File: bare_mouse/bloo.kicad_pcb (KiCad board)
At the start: 2 copper layers, 100 x 105.9 mm, 99 parts, among them J1 Serial Debug Header, J10 Conn_01x06_Female, J2 SWD Header, J4 Conn_ARM_JTAG_SWD_10, J5 SWD Header, M1 M1_Conn_Alt, M2 M2_Conn_Alt, Q0 TEFT4300, Q1 TEFT4300, Q10 Q_NMOS_GSD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

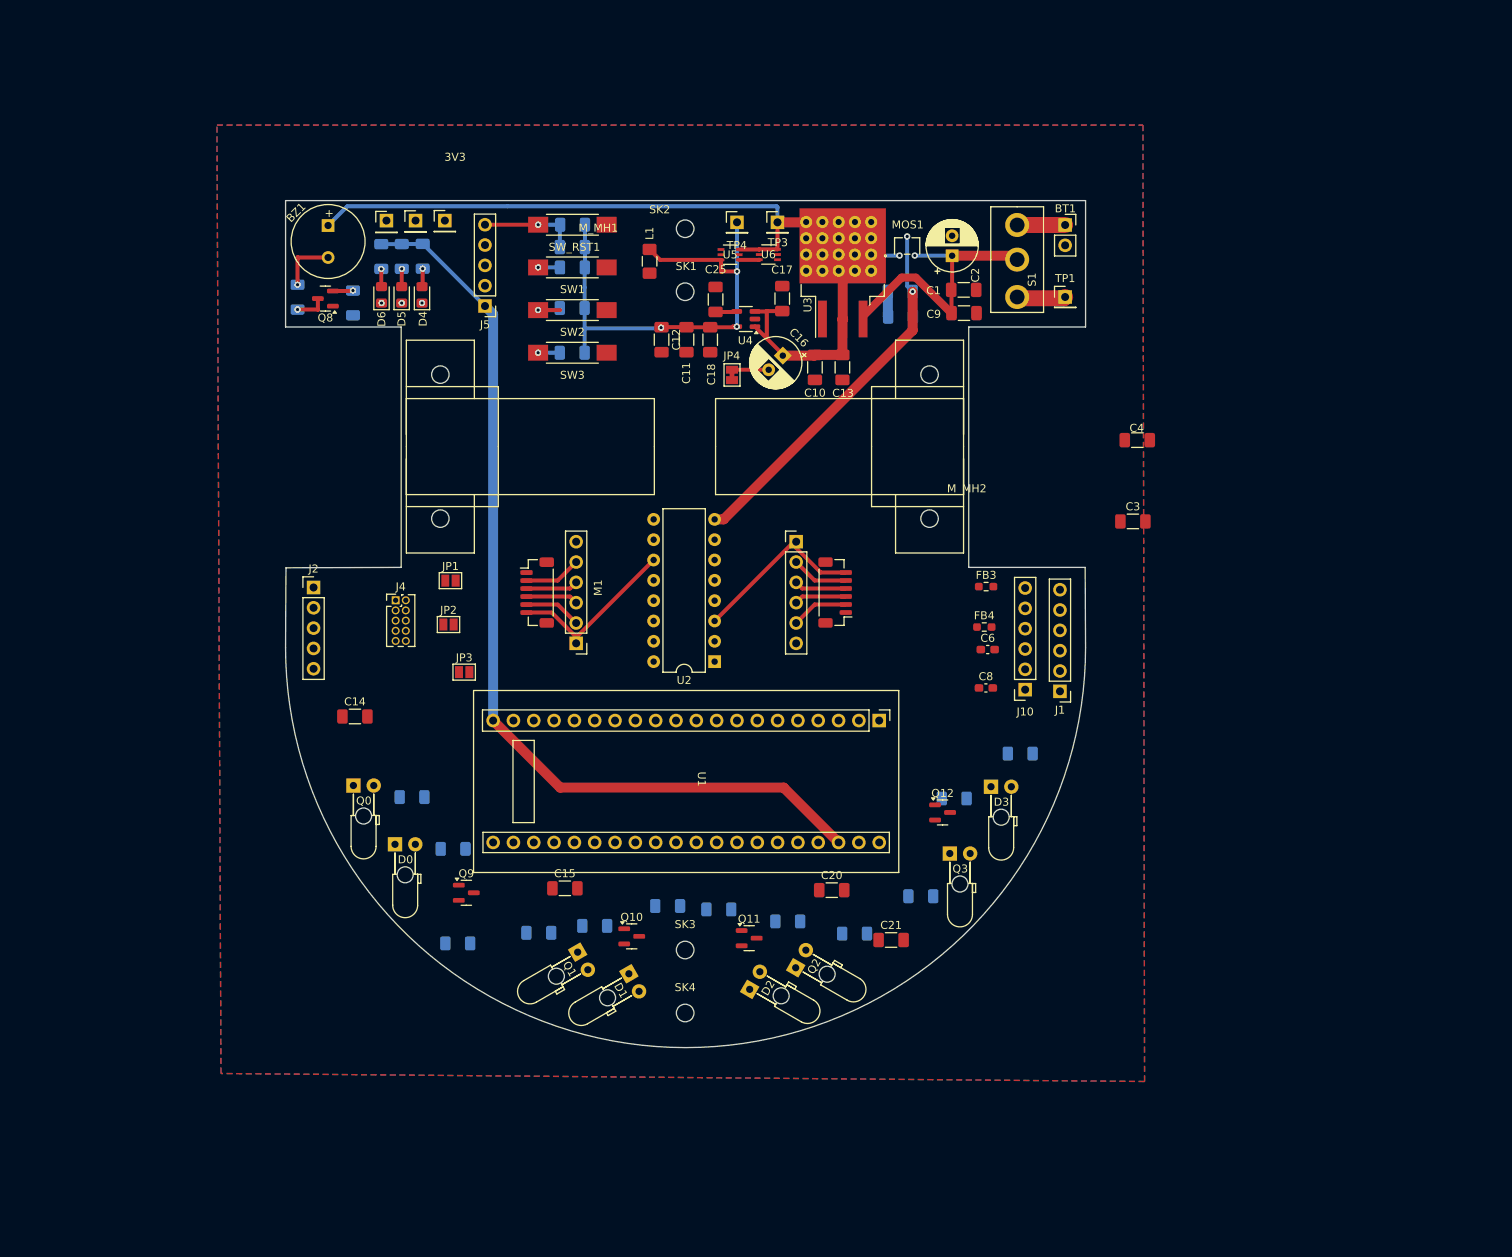
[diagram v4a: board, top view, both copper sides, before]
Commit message: Finished routing, DRC shows 8 errors having to do with SWD header module
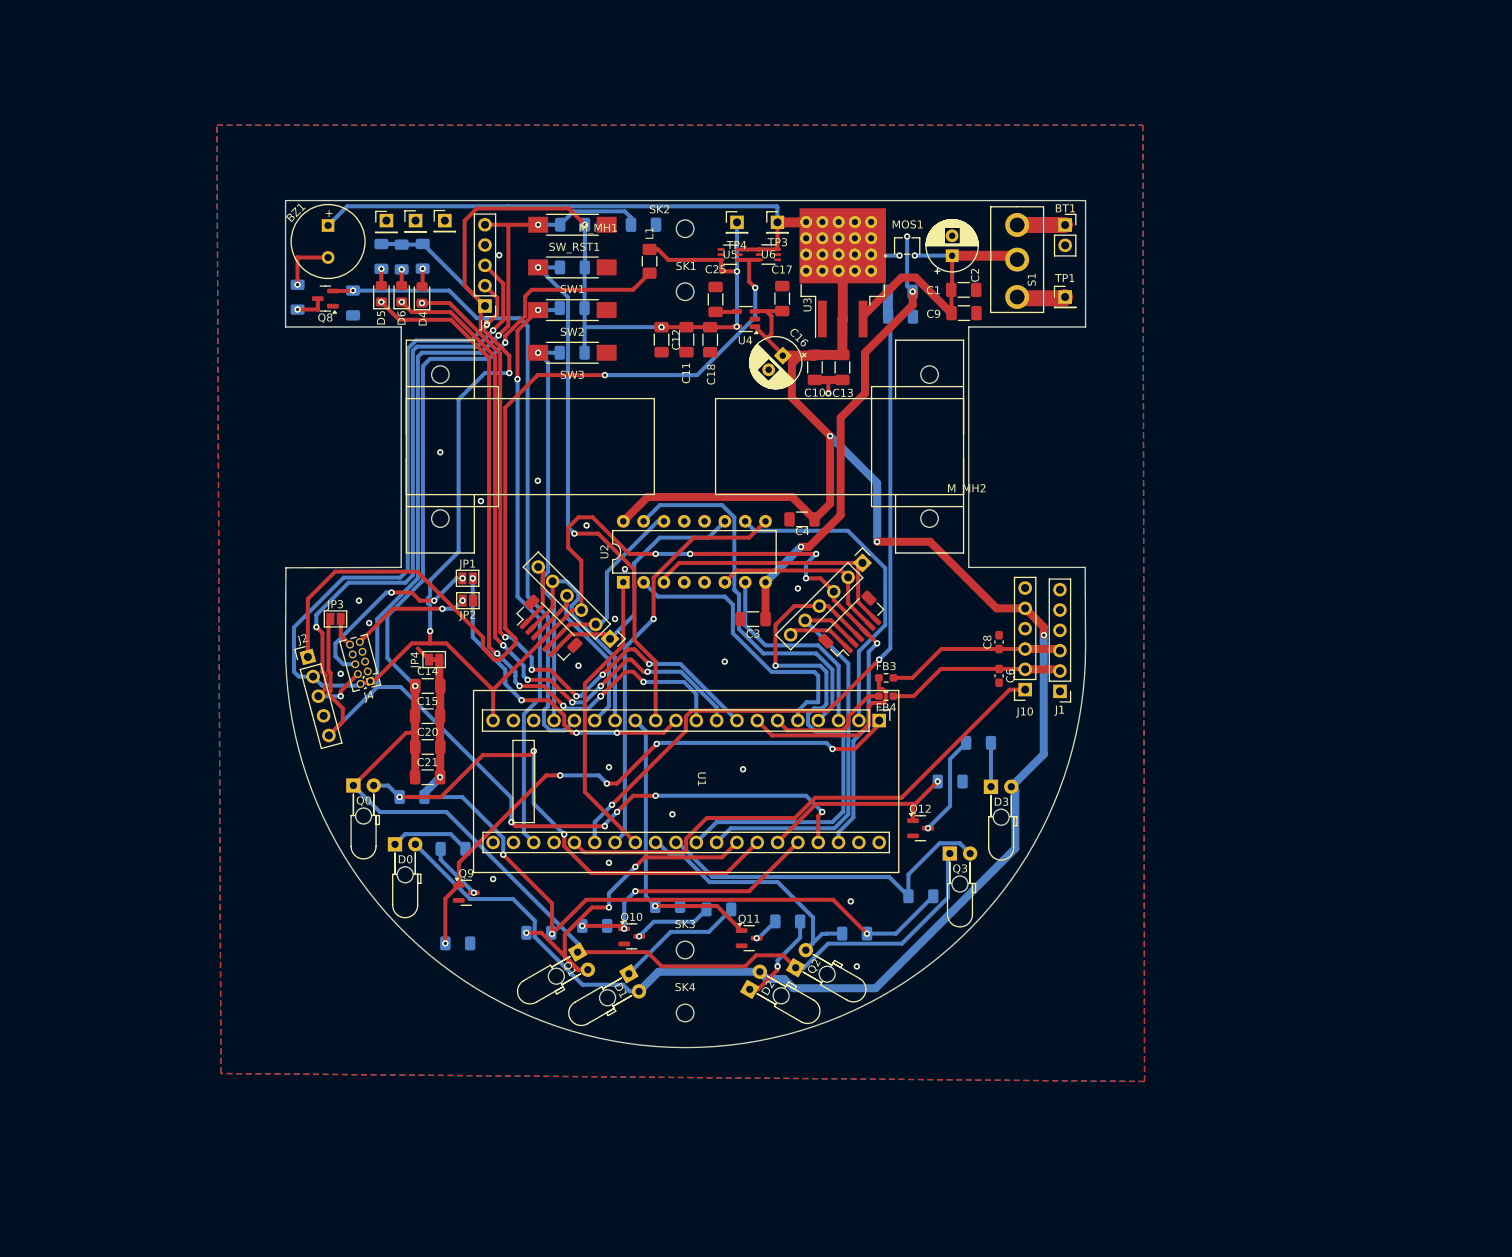
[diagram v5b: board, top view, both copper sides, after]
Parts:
- moved C21 61.4 mm to (178.5, 162.5)
- moved C20 53.6 mm to (178.5, 158.8)
- moved JP4 51.5 mm to (179.3, 147.8), turned to 0 degrees
- moved C3 49.0 mm to (219.2, 142.8), turned to 180 degrees
- moved C4 43.1 mm to (225.3, 130.3), turned to 180 degrees
- moved C15 27.5 mm to (178.5, 154.9)
- moved JP3 17.4 mm to (167.0, 142.7)
- moved FB3 16.9 mm to (235.8, 150.1)
- moved U2 15.1 mm to (203.0, 138.2), turned to 90 degrees
- moved FB4 15.0 mm to (235.8, 152.4), turned to 180 degrees
- moved J4 10.6 mm to (171.3, 150.5), turned to -165 degrees
- moved C14 9.87 mm to (178.5, 151.1)
- moved C19 9.32 mm to (205.5, 93.5)
- moved J2 8.71 mm to (163.5, 147.5), turned to 15 degrees
- moved C8 5.97 mm to (249.9, 145.6), turned to 90 degrees
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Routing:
- net +5V_NET: track 106.1 -> 320.0 mm, vias 1 -> 4
- net +3.3VA: track 0.00 -> 195.0 mm, vias 0 -> 2
- net RST: track 12.2 -> 185.5 mm, vias 1 -> 7
- net +3V3_NET: track 2.52 -> 116.8 mm, vias 0 -> 2
- net AGND: track 0.00 -> 97.7 mm, vias 0 -> 4
- net +3V3: track 192.3 -> 284.2 mm, vias 3 -> 11
- net V_METER: track 3.15 -> 94.5 mm, vias 0 -> 2
- net LED_GREEN: track 0.00 -> 88.7 mm, vias 1 -> 7
- net LED_BLUE: track 0.00 -> 87.7 mm, vias 1 -> 6
- net LED_RED: track 0.00 -> 87.1 mm, vias 1 -> 6
- net SWDCLK: track 0.00 -> 80.3 mm, vias 0 -> 3
- net BUZZER: track 2.53 -> 81.9 mm
- net SWDIO: track 0.00 -> 76.7 mm, vias 0 -> 1
- net EMIT_1: track 0.00 -> 72.6 mm, vias 0 -> 5
- net BUTTON_2: track 5.57 -> 73.5 mm, vias 1 -> 2
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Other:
- board text removed: "3V3"

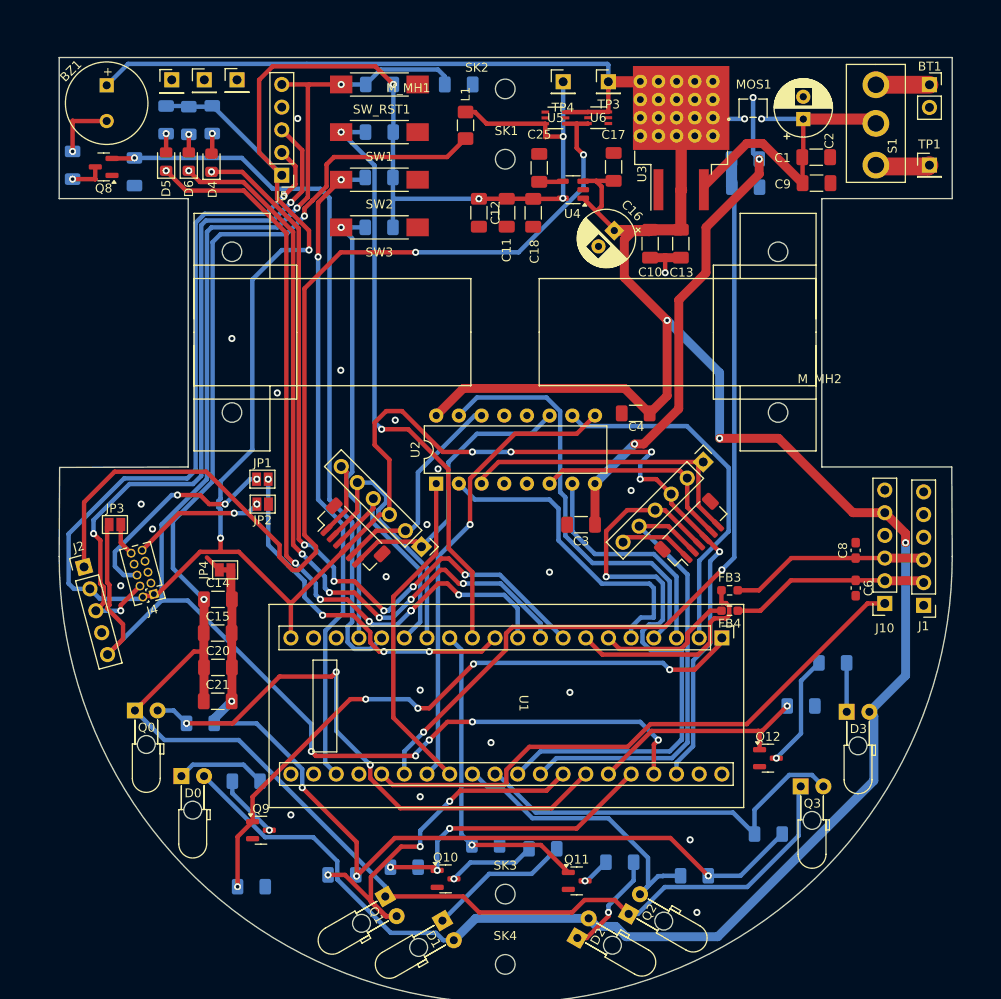
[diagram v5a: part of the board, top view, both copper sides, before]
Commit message: Finished routing the mouse, referenced design notes to finalize silkscreen, rearranged SWD header module to fix previous errors - current final draft of the rat
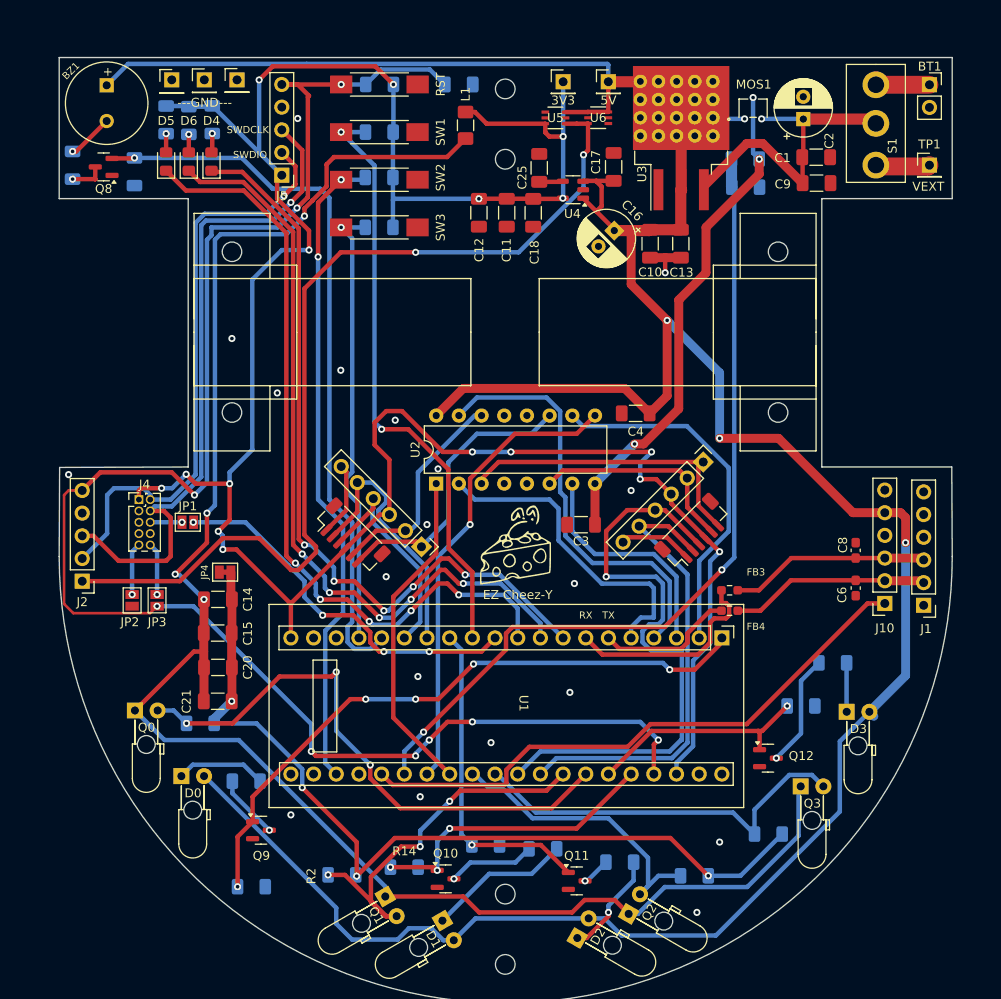
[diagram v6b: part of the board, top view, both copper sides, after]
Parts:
- added G***: LOGO, LOGO, F.Cu at (211.8, 145.7)
- moved JP2 18.2 mm to (168.9, 151.2), turned to 90 degrees
- moved J4 10.7 mm to (169.7, 140.0), turned to 0 degrees
- moved JP3 9.71 mm to (171.7, 151.2), turned to 90 degrees
- moved JP1 9.65 mm to (175.1, 142.5)
- moved J2 1.61 mm to (163.3, 149.1), turned to 180 degrees
- moved JP4 0.25 mm to (179.3, 148.1)
- moved D4 0.13 mm to (177.8, 102.1)
- renumbered SW_RST1 to RST
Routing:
- net Net-(J4-SWO/TDO): track 24.6 -> 3.56 mm, vias 3 -> 1
- net SWDIO: track 76.7 -> 65.8 mm
- net +3V3_NET: track 116.8 -> 106.4 mm
- net Net-(J4-GNDDetect): track 15.0 -> 5.87 mm, vias 2 -> 1
- net SWDCLK: track 80.3 -> 74.4 mm, vias 3 -> 1
- net RST: track 185.5 -> 189.4 mm, vias 7 -> 9
- net +3V3: track 284.2 -> 281.8 mm, vias 11 -> 16
- net Net-(J4-~{RESET}): track 3.69 -> 5.87 mm, vias 0 -> 1
- net SWO: track 40.1 -> 42.2 mm
- net Net-(BZ1-+): track 7.27 -> 5.23 mm
- net GND: track 23.6 -> 21.6 mm, vias 18 -> 19
- net +5V_NET: track 320.0 -> 321.4 mm
- net EMIT_1: track 72.6 -> 71.8 mm
- net LED_RED: track 87.1 -> 87.2 mm, vias 6 -> 5
- net +3.3VA: track 195.0 -> 195.1 mm, vias 2 -> 4
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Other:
- board text added: "---GND---"
- board text added: "3V3"
- board text added: "5V"
- board text added: "Anthony Ahn Joel Akiyoshi Justin Grino"
- board text added: "EZ Cheez-Y"
- board text added: "EZ Cheezy Team:"
- board text added: "RX"
- board text added: "SWDCLK"
- board text added: "SWDIO"
- board text added: "TX"
- board text added: "VEXT"
